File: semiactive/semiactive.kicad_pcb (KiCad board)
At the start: 2 copper layers, 86.6 x 100.8 mm, 2 parts, among them J4 5223002-2, U1 Teensy4.1

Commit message: Create a few projects
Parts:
- added C1: C, Capacitor_SMD:C_0603_1608Metric, F.Cu at (164.2, 43.6)
- added C2: C, Capacitor_SMD:C_0603_1608Metric, F.Cu at (173.2, 43.6)
- added C3: C, Capacitor_SMD:C_0603_1608Metric, F.Cu at (182.3, 43.7)
- added C4: 10uF, Capacitor_SMD:C_0603_1608Metric, F.Cu at (239.3, 70.6)
- added C6: .1uF, Capacitor_SMD:C_0402_1005Metric, F.Cu at (241.6, 71.1)
- added C7: 1uF, Capacitor_SMD:C_0402_1005Metric, F.Cu at (240.5, 71.1)
- added D1: SET.F, !footprints:LED_IN-PI42TASPRPGPB, F.Cu at (168.6, 42.5)
- added D2: SET.R, !footprints:LED_IN-PI42TASPRPGPB, F.Cu at (177.8, 42.6)
- added D3: STATUS, !footprints:LED_IN-PI42TASPRPGPB, F.Cu at (187.3, 42.6)
- added D4: SET.F, !footprints:LED_WS2812B_PLCC4_5.0x5.0mm_P3.2mm, B.Cu at (168.7, 44.2)
- added D5: SET.R, !footprints:LED_WS2812B_PLCC4_5.0x5.0mm_P3.2mm, B.Cu at (177.7, 44.2)
- added D6: STATUS, !footprints:LED_WS2812B_PLCC4_5.0x5.0mm_P3.2mm, B.Cu at (187.2, 44.2)
- added U2: ESP8266EX, Package_DFN_QFN:QFN-32-1EP_5x5mm_P0.5mm_EP3.45x3.45mm, F.Cu at (245.1, 73.6)
- J4: footprint 5223002-2:TE_5223002-2 -> !footprints:52230042
- U1: footprint teensy:Teensy41 -> !footprints:Teensy41
- moved U1 30.7 mm to (153.4, 73.7)
- moved J4 18.1 mm to (187.4, 111.2)
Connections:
- U1 pad 7: unconnected-(U1-Pad7) -> ARGBLED
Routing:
- net VOLT1: track 0.00 -> 82.9 mm
- net VOLT2: track 0.00 -> 80.6 mm
- net TX: track 0.00 -> 78.8 mm
- net RX: track 0.00 -> 75.5 mm
- net ARGBLED: track 0.00 -> 36.6 mm
- net 5V: track 0.00 -> 3.59 mm
- added copper zone on B.Cu, net GND
- added copper zone on F.Cu, net GND
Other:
- board size 86.6 x 100.8 mm -> 85 x 85 mm

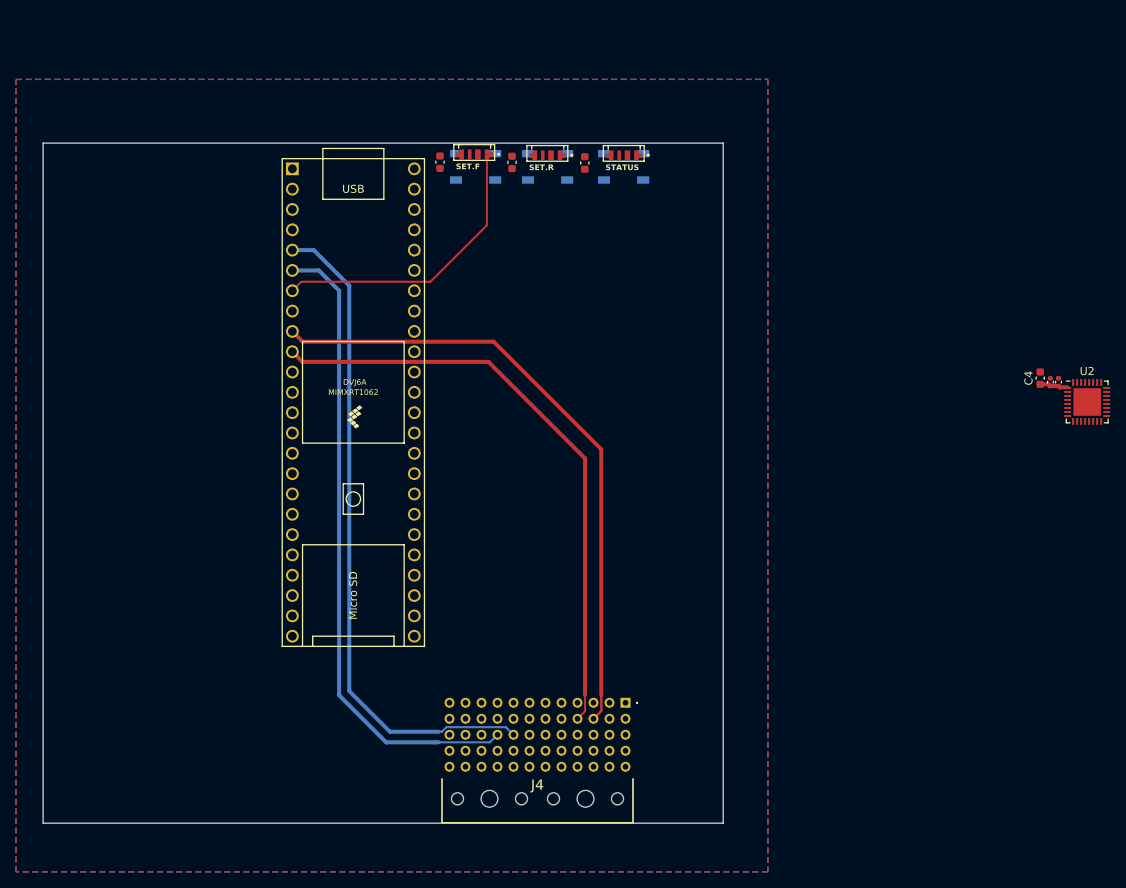
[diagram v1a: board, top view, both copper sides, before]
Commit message: Route SAS board
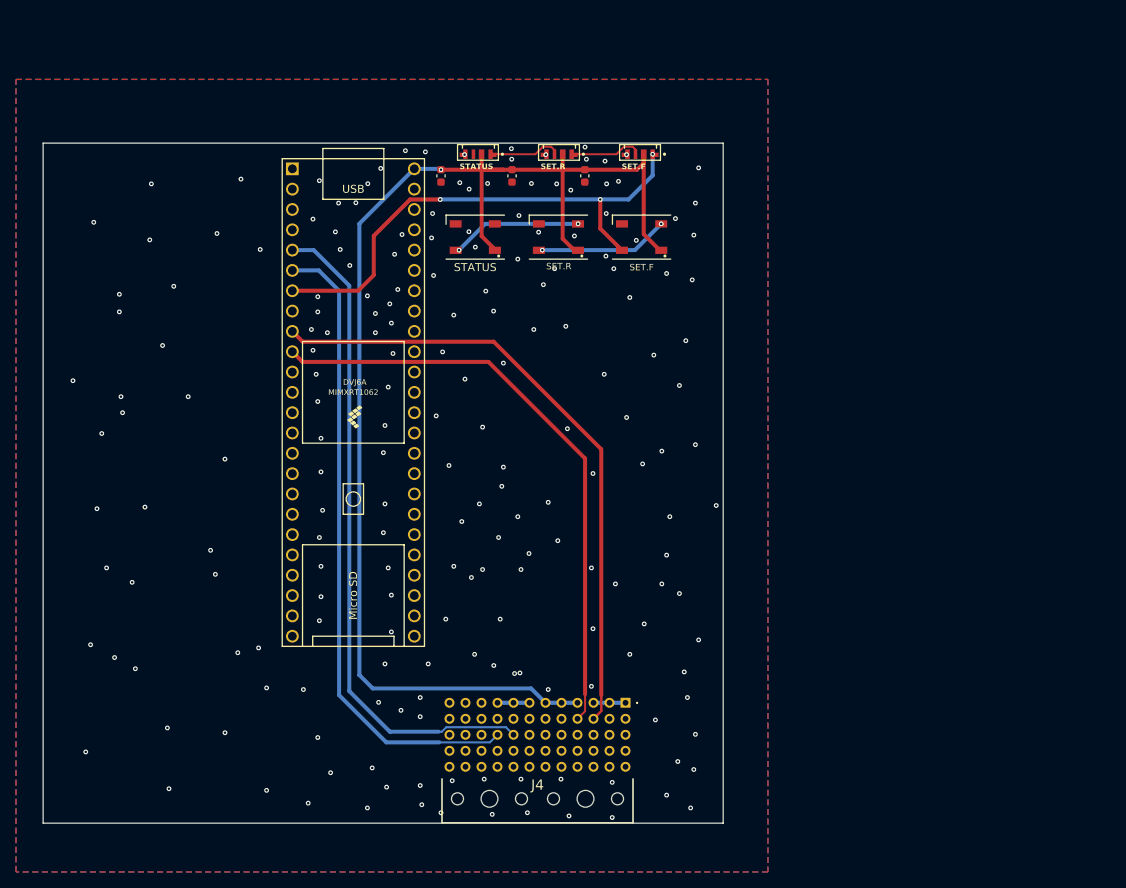
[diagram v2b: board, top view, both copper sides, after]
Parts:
- removed C4: 10uF, Capacitor_SMD:C_0603_1608Metric
- removed C6: .1uF, Capacitor_SMD:C_0402_1005Metric
- removed C7: 1uF, Capacitor_SMD:C_0402_1005Metric
- removed U2: ESP8266EX, Package_DFN_QFN:QFN-32-1EP_5x5mm_P0.5mm_EP3.45x3.45mm
- D4, D5, D6: moved to F.Cu
- moved D4 22.5 mm to (189.4, 53.0)
- moved D1 20.7 mm to (189.3, 42.5)
- moved D6 20.5 mm to (168.7, 53.0)
- moved D3 18.2 mm to (169.1, 42.5)
- moved D5 8.89 mm to (179.1, 53.0)
- moved C1 1.72 mm to (164.4, 45.3)
- moved C2 1.69 mm to (173.2, 45.3)
- moved C3 1.61 mm to (182.3, 45.3)
- moved D2 1.46 mm to (179.2, 42.5)
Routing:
- net 5V: track 3.59 -> 165.9 mm, vias 0 -> 1
- net ARGBLED: track 36.6 -> 64.0 mm, vias 0 -> 3
- net Net-(D5-DOUT): track 0.00 -> 16.2 mm, vias 0 -> 2
- net Net-(D4-DOUT): track 0.00 -> 16.2 mm, vias 0 -> 2
- net Net-(D1-DOUT): track 0.00 -> 9.09 mm
- net Net-(D2-DOUT): track 0.00 -> 9.05 mm
- net 8.4V: track 0.00 -> 4.00 mm
- net 3.3V: track 0.00 -> 4.00 mm
- net VOLT2: track 80.6 -> 80.1 mm
- net RX: track 75.5 -> 75.0 mm
- net GND: vias 0 -> 199

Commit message: Aesthetic SAS updates
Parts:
- moved C3 6.39 mm to (188.7, 45.8), turned to 180 degrees
- moved C2 5.33 mm to (178.6, 45.7), turned to 180 degrees
- moved C1 3.92 mm to (168.3, 45.7), turned to 180 degrees
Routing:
- net 5V: track 165.9 -> 167.0 mm, vias 1 -> 0
- net GND: vias 199 -> 203

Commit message: SAS: Small changes
Should be all routed and ready to go...
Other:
- board text added: "SAS-2308 Designed by D.C."
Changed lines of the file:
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@@
   (gr_line (start 199.644 126.238) (end 199.644 41.23802)
     (stroke (width 0.254) (type solid)) (layer "User.1"))
+  (gr_text "SAS-2308\nDesigned by D.C.\n" (at 116.205 124.968) (layer "F.SilkS")
+    (effects (font (size 1.5 1.5) (thickness 0.3) bold) (justify left bottom))
+  )
   (segment (start 189.7068 52.6188) (end 189.7068 42.6244) (width 0.5) (layer "F.Cu") (net 1))
   (segment (start 182.348 44.559) (end 188.8722 44.559) (width 0.5) (layer "F.Cu") (net 1))
@@
   (segment (start 169.9 51.334) (end 181.5015 51.334) (width 0.5) (layer "B.Cu") (net 11))
   (segment (start 166.624 54.61) (end 169.9 51.334) (width 0.5) (layer "B.Cu") (net 11))
+  (segment (start 186.997 54.634) (end 184.941 52.578) (width 0.5) (layer "F.Cu") (net 52))
   (segment (start 159.258 49.540234) (end 159.258 49.53) (width 0.5) (layer "F.Cu") (net 52))
   (segment (start 145.796 59.69) (end 154.016 59.69) (width 0.5) (layer "F.Cu") (net 52))
   (segment (start 155.972 57.734) (end 155.972 52.826233) (width 0.5) (layer "F.Cu") (net 52))
   (segment (start 159.199617 49.598617) (end 159.258 49.540234) (width 0.5) (layer "F.Cu") (net 52))
-  (segment (start 186.006 53.643) (end 185.957 53.594) (width 0.5) (layer "F.Cu") (net 52))
+  (segment (start 184.941 52.578) (end 184.912 52.578) (width 0.5) (layer "F.Cu") (net 52))
   (segment (start 154.016 59.69) (end 155.972 57.734) (width 0.5) (layer "F.Cu") (net 52))
-  (segment (start 186.997 54.634) (end 186.006 53.643) (width 0.5) (layer "F.Cu") (net 52))
-  (segment (start 185.957 53.594) (end 185.928 53.594) (width 0.5) (layer "F.Cu") (net 52))
   (segment (start 155.972 52.826233) (end 159.199617 49.598617) (width 0.5) (layer "F.Cu") (net 52))
   (via (at 159.258 49.53) (size 0.6) (drill 0.3) (layers "F.Cu" "B.Cu") (net 52))
-  (via (at 185.928 53.594) (size 0.6) (drill 0.3) (layers "F.Cu" "B.Cu") (net 52))
+  (via (at 184.912 52.578) (size 0.6) (drill 0.3) (layers "F.Cu" "B.Cu") (net 52))
   (via (at 190.8318 42.6244) (size 0.6) (drill 0.3) (layers "F.Cu" "B.Cu") (net 52))
   (segment (start 184.297 48.26) (end 187.846 48.26) (width 0.5) (layer "B.Cu") (net 52))
-  (segment (start 184.277 51.943) (end 184.277 48.28) (width 0.5) (layer "B.Cu") (net 52))
   (segment (start 190.8318 45.2742) (end 190.8318 42.6244) (width 0.5) (layer "B.Cu") (net 52))
   (segment (start 184.277 48.28) (end 184.297 48.26) (width 0.5) (layer "B.Cu") (net 52))
@@
   (segment (start 187.846 48.26) (end 190.8318 45.2742) (width 0.5) (layer "B.Cu") (net 52))
   (segment (start 160.508 48.28) (end 159.258 49.53) (width 0.5) (layer "B.Cu") (net 52))
-  (segment (start 185.928 53.594) (end 184.277 51.943) (width 0.5) (layer "B.Cu") (net 52))
+  (segment (start 184.277 48.28) (end 184.277 51.943) (width 0.5) (layer "B.Cu") (net 52))
+  (segment (start 184.277 51.943) (end 184.912 52.578) (width 0.5) (layer "B.Cu") (net 52))
   (segment (start 183.434 111.19) (end 187.434 111.19) (width 0.5) (layer "B.Cu") (net 53))
   (segment (start 175.434 111.19) (end 171.434 111.19) (width 0.5) (layer "B.Cu") (net 54))

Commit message: Easter eggs
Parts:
- removed J4: 5223002-2, !footprints:52230042
- added G***: LOGO, LOGO, F.Cu at (181.1, 80.8)
- added J1: 5223004-2, !footprints:52230042, F.Cu at (187.5, 111.2)
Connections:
- U1 pad 10: RX -> CVT_RX_DAQ_TX
- U1 pad 5: VOLT1 -> SOLENOID_PWM_1
- U1 pad 6: VOLT2 -> SOLENOID_PWM_2
- U1 pad 9: TX -> CVT_TX_DAQ_RX
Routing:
- net VOLT1: track 82.9 -> 0.00 mm
- net CVT_TX_DAQ_RX: track 0.00 -> 82.8 mm
- net SOLENOID_PWM_1: track 0.00 -> 80.5 mm
- net VOLT2: track 80.1 -> 0.00 mm
- net CVT_RX_DAQ_TX: track 0.00 -> 79.0 mm
- net TX: track 78.8 -> 0.00 mm
- net SOLENOID_PWM_2: track 0.00 -> 78.1 mm
- net RX: track 75.0 -> 0.00 mm
- net 5V: track 167.0 -> 175.3 mm, vias 0 -> 2
- net 8.4V: track 4.00 -> 0.00 mm
- net 3.3V: track 4.00 -> 0.00 mm
- net +3V3: track 0.00 -> 4.00 mm
- net GND: vias 203 -> 210
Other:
- board text added: "SAAAAAAAAAAAAAAAAAAAAAAAAAAAAAAAAAAAAAAAAAAAAAAAAAAAAAAAAS"
- board text added: "There are no components; only profound statements."
- board text added: "{dblquote}Andrew has very squeezable boobs{dblquote} @Joe Keenan"
- board text added: "{dblquote}As long as there are no human remains still in it, a free tub is a free tub.{dblquote} - @Michael McDowell"
- board text added: "{dblquote}Buy an E-Bike stop being poor{dblquote} - @Logan Wershing"
- board text added: "{dblquote}Does all of SLO smell like shit or did I just crap my pants?{dblquote} - @Fricheal Meeman"
- board text added: "{dblquote}How do you open this? I've never had a dishwasher{dblquote} - @Will Duncan (Winner of the Will Duncan award)"
- board text added: "{dblquote}I just rub myself in purell every morning{dblquote} - @Jiyen Northan"
- board text added: "{dblquote}I may not know how to spell 'hydrodynamics', but I sure know how to catch a big ol' fish with a beer in hand.{dblquote} - @Joshua Wright"
- board text added: "{dblquote}I wanna see Josh in lingerie{dblquote} - @Harry"
- board text added: "{dblquote}I'm a woman in STEM. That's a hate crime…{dblquote} - @Sarah Talbert"
- board text added: "{dblquote}I'm gonna start waterjetting the urinal{dblquote} - @David Rank"
- board text added: "{dblquote}If I have to listen to Mr. Brightside one more time, I'm going to shoot myself in the knee cap{dblquote} - @Tator"
- board text added: "{dblquote}Laurenitis{dblquote} - @Lauren Jones"
- board text added: "{dblquote}MILF slayer energy{dblquote} - @lucia"
- board text added: "{dblquote}My teeth were also not in it which is kind of the problem{dblquote} - @Jay Kahling"
- board text added: "{dblquote}Often times when I'm nice I regret it later{dblquote} - @SydneyFW"
- board text added: "{dblquote}Pickels are my favorite quote unquote 'vegetable' {dblquote} - @Colin Williams"
- board text added: "{dblquote}Smuggling is a hobby{dblquote} - @Thad"
- board text added: "{dblquote}The best way to improve our team's performance is illegal drugs{dblquote} - @Ben"
- board text added: "{dblquote}There's no such thing; women don't exist.{dblquote} - @Ethan Mikel"
- board text added: "{dblquote}They call me the one pump chump{dblquote} - @Elijah Gordon"
- board text added: "{dblquote}Who the fuck pissed my pants{dblquote} - @Carter Foye"
- board text added: "{dblquote}meow{dblquote} - @Andrew Whitacre"

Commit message: Update semiactive ponkerman
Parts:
- moved G*** 1.83 mm to (182.1, 82.3)
